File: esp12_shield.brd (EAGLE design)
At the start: 50 x 50 mm, 30 parts, among them CN1 1X4-CLEANBIG, CN2 1X4-CLEANBIG, CN3 1X4-CLEANBIG, IC1 117\33

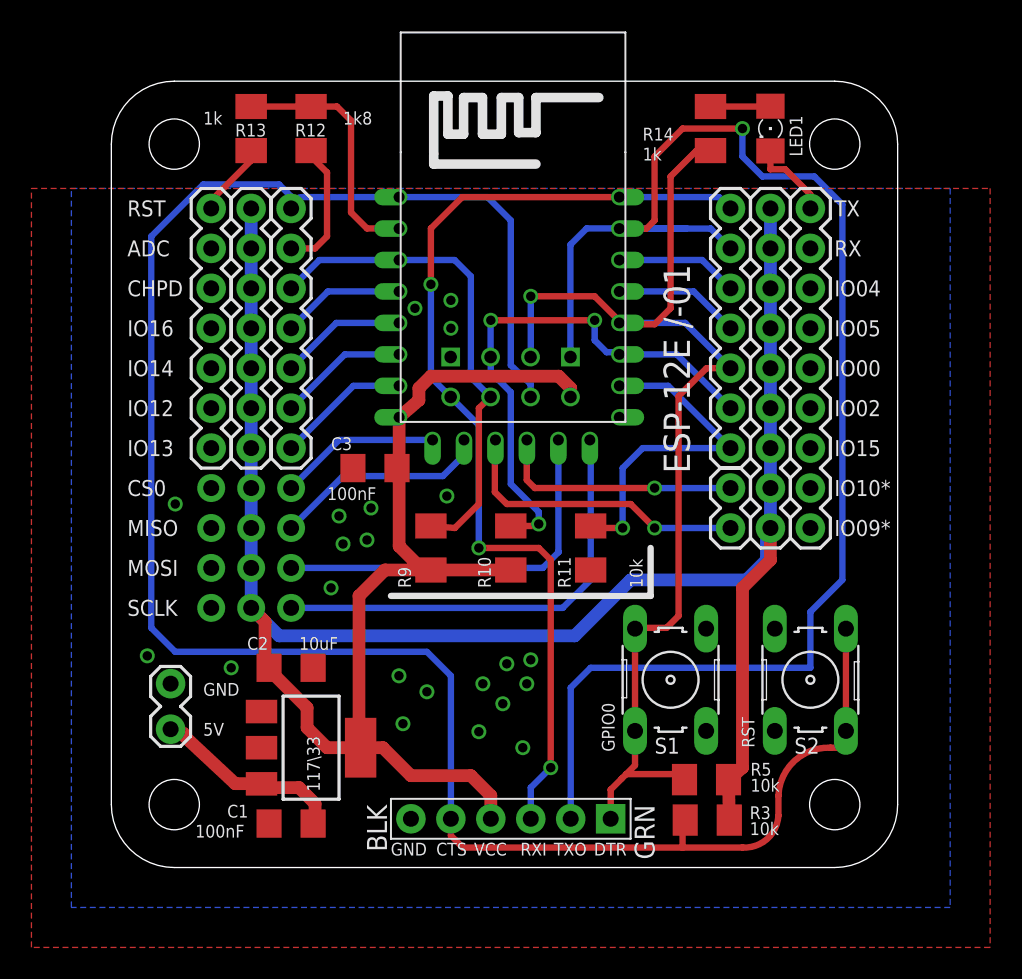
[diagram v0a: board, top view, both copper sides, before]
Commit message: shield added
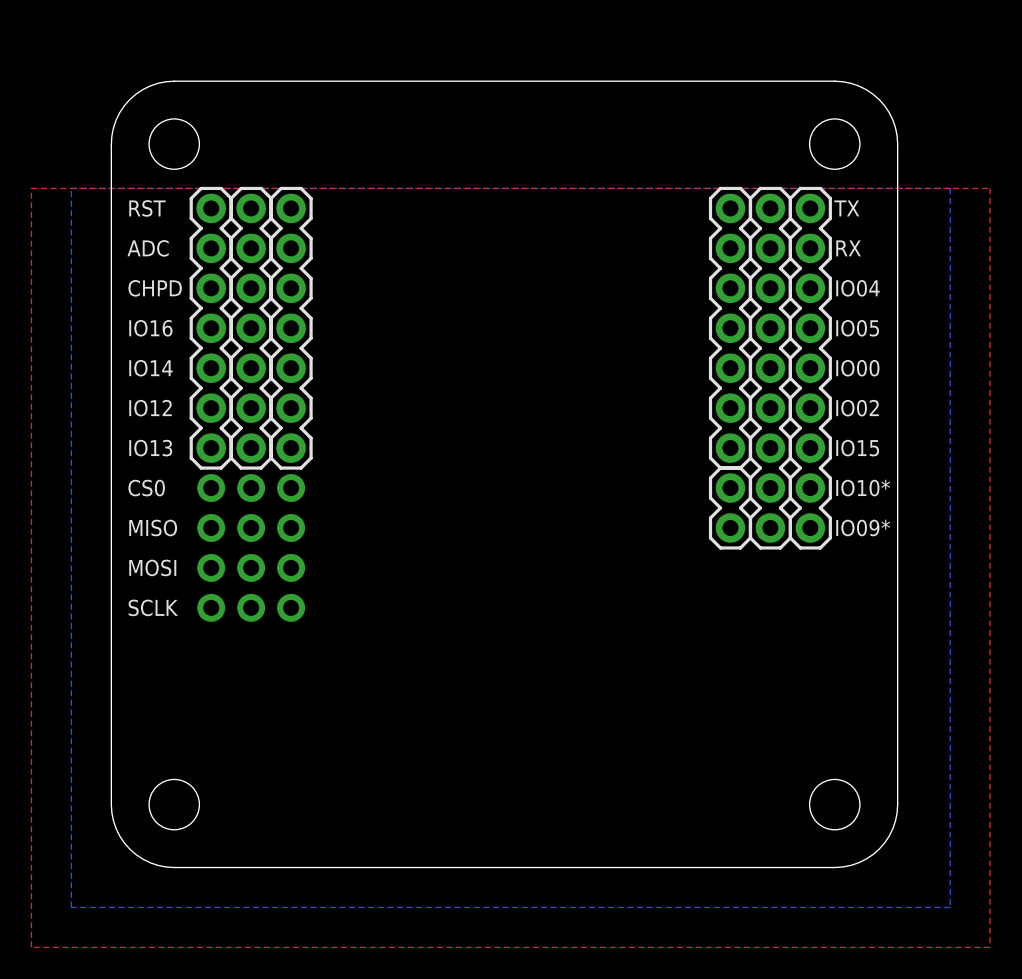
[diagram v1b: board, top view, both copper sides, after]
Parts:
- removed C1, C3: 100nF, resistor:C1206
- removed C2: 10uF, resistor:C1206
- removed IC1: 117\33, v-reg:SOT223
- removed JP1: FTDI_DEVICE, SparkFun-Connectors:FTDI_DEVICE_SIDE
- removed JP2: M02LOCK, SparkFun-Connectors:1X02_LOCK
- removed LED1: (no value), led:1206
- removed R10, R11, R3, R5, R9: 10k, resistor:M1206
- removed R12: 1k8, resistor:M1206
- removed R13, R14: 1k, resistor:M1206
- removed S1: GPIO0, switch-omron:B3F-10XX
- removed S2: RST, switch-omron:B3F-10XX
- removed U$2: ESP01, esp8266modules:ESP01
- removed U$3: ESP-12E /-01, esp8266modules:ESP12E
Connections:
- removed net ADC: R12.2, R13.1, U$3.ADC
- removed net N$8: LED1.A, R14.1
- removed net N$9: JP4.6, R12.1
- removed net VCC: C1.2, IC1.3, JP2.1
- net +3V3: no longer C2.2, C3.2, IC1.4, JP1.P$4, R10.1, R3.1, R5.1, R9.1, U$2.VCC, U$3.VCC
- net CH_PD: no longer R9.2, U$2.CH_PD, U$3.CH_PD
- net FRX_ETX: no longer JP1.P$3, U$2.TX, U$3.TX
- net FTX_ERX: no longer JP1.P$2, U$2.RX, U$3.RX
- net GND: no longer C1.1, C2.1, C3.1, IC1.1, JP1.P$6, JP2.2, LED1.C, R11.1, R13.2, S1.1, S1.2, S2.1, S2.2, U$2.GND, U$3.GND
- net GPIO0: no longer JP1.P$1, R14.2, R5.2, S1.3, S1.4, U$2.GPIO0, U$3.GPIO0
- net GPIO15: no longer R11.2, U$3.GPIO15
- net GPIO2: no longer R10.2, U$2.GPIO2, U$3.GPIO2
- net N$1: no longer JP1.P$5, R3.2, S2.3, S2.4, U$2.RST, U$3.RESET
- net N$10: no longer U$3.MOSI
- net N$11: no longer U$3.SCLK
- net N$14: no longer U$3.GPIO5
- net N$15: no longer U$3.GPIO4
- net N$16: no longer U$3.GPIO9
- net N$17: no longer U$3.GPIO10
- net N$2: no longer U$3.CS0
- net N$3: no longer U$3.GPIO13
- net N$4: no longer U$3.GPIO12
- net N$5: no longer U$3.GPIO14
- net N$6: no longer U$3.MISO
- net N$7: no longer U$3.GPIO16
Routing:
- net +3V3: track 175.0 -> 0.00 mm
- net N$1: track 131.4 -> 0.00 mm
- net FTX_ERX: track 100.0 -> 0.00 mm, vias 1 -> 0
- net GPIO0: track 71.8 -> 0.00 mm, vias 1 -> 0
- net FRX_ETX: track 63.6 -> 0.00 mm, vias 3 -> 0
- net GPIO2: track 34.4 -> 0.00 mm, vias 3 -> 0
- net CH_PD: track 31.6 -> 0.00 mm
- net N$11: track 28.7 -> 0.00 mm
- net N$10: track 24.6 -> 0.00 mm
- net GPIO15: track 22.0 -> 0.00 mm, vias 1 -> 0
- net N$16: track 19.3 -> 0.00 mm, vias 1 -> 0
- net ADC: track 16.0 -> 0.00 mm
- net N$17: track 15.7 -> 0.00 mm, vias 1 -> 0
- net N$6: track 13.9 -> 0.00 mm
- net VCC: track 13.9 -> 0.00 mm
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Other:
- board text removed: "100nF"
- board text removed: "5V"
- board text removed: "GND"
